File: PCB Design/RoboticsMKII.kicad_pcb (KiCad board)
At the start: 4 copper layers, 93 parts, among them CON1 USB, CON2 BARREL_JACK, P1 Power Sel, P10 CONN_02X12, P11 DAC, P12 Reed, P13 SPI, P14 ICSP, P15 Gnd, P16 UART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

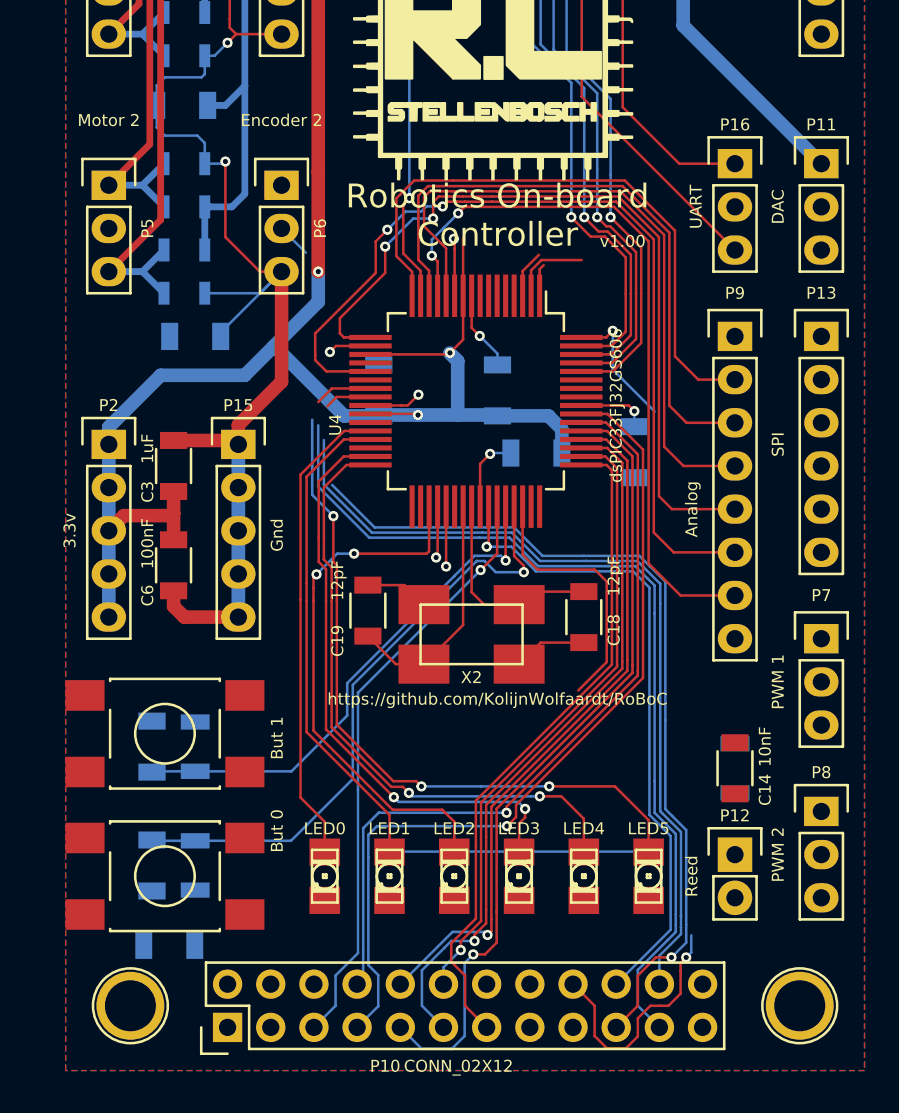
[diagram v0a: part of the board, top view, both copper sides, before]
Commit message: More done. PWM and SPI need attention
Signed-off-by: Kolijn Wolfaardt <kolijn.wolfaardt@gmail.com>
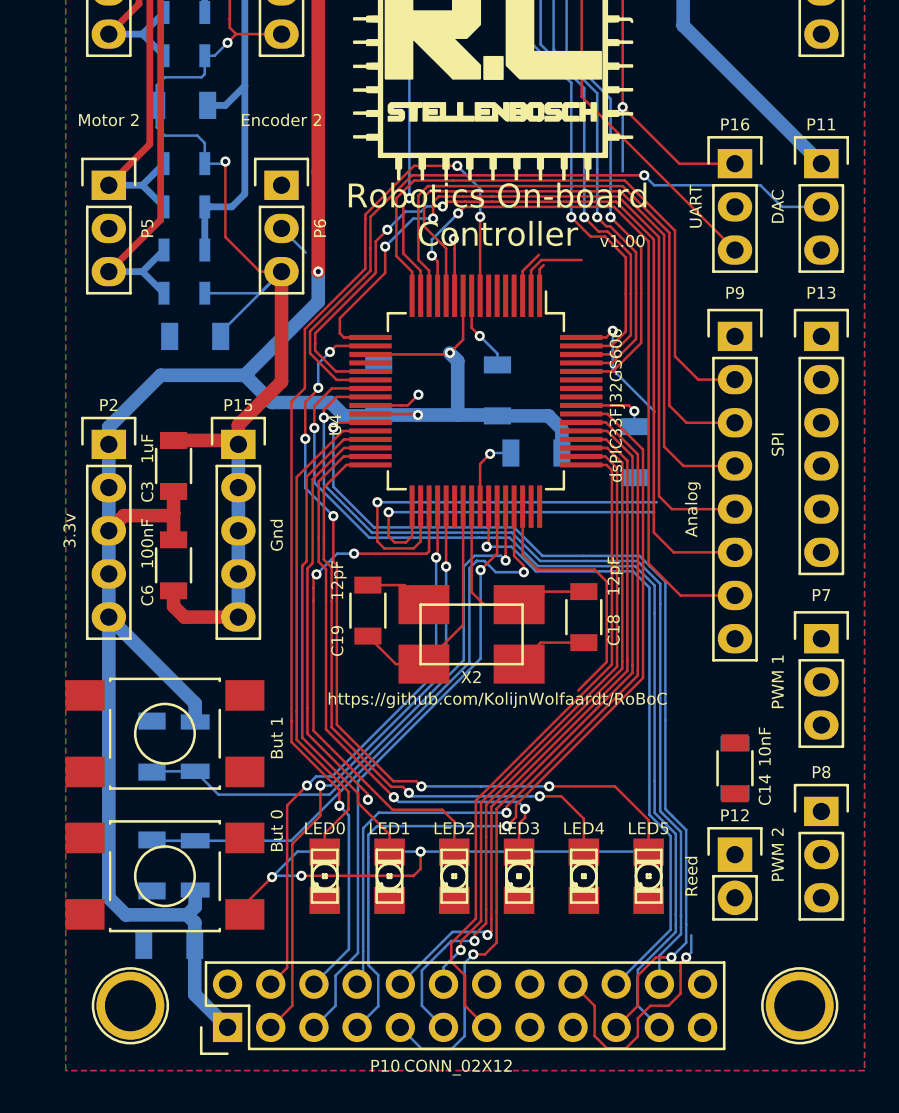
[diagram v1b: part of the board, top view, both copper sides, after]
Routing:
- net /gpio/Href: track 0.00 -> 64.1 mm, vias 0 -> 3
- net /gpio/DACOUT: track 0.00 -> 42.0 mm, vias 0 -> 1
- net V3.3: track 258.2 -> 294.9 mm
- net /gpio/SIO_C: track 3.53 -> 35.3 mm, vias 1 -> 2
- net /gpio/SIO_D: track 3.05 -> 32.7 mm, vias 1 -> 2
- net /usb/MCU_RX: track 28.2 -> 55.6 mm, vias 1 -> 3
- net /gpio/Reed: track 0.00 -> 24.6 mm, vias 0 -> 1
- net /usb/MCU_TX: track 33.5 -> 53.9 mm, vias 1 -> 2
- net GND: track 237.0 -> 254.1 mm, vias 14 -> 17
- net /gpio/~WR: track 50.9 -> 56.6 mm, vias 1 -> 2
- net /gpio/LED5: track 44.1 -> 48.9 mm, vias 4 -> 6
- net /gpio/BUT_1: track 30.5 -> 33.7 mm
- net /gpio/~RRST: track 52.2 -> 54.2 mm, vias 0 -> 1
- net /gpio/~WRST: track 57.2 -> 58.7 mm, vias 0 -> 1
- net /gpio/LED0: track 28.0 -> 29.4 mm

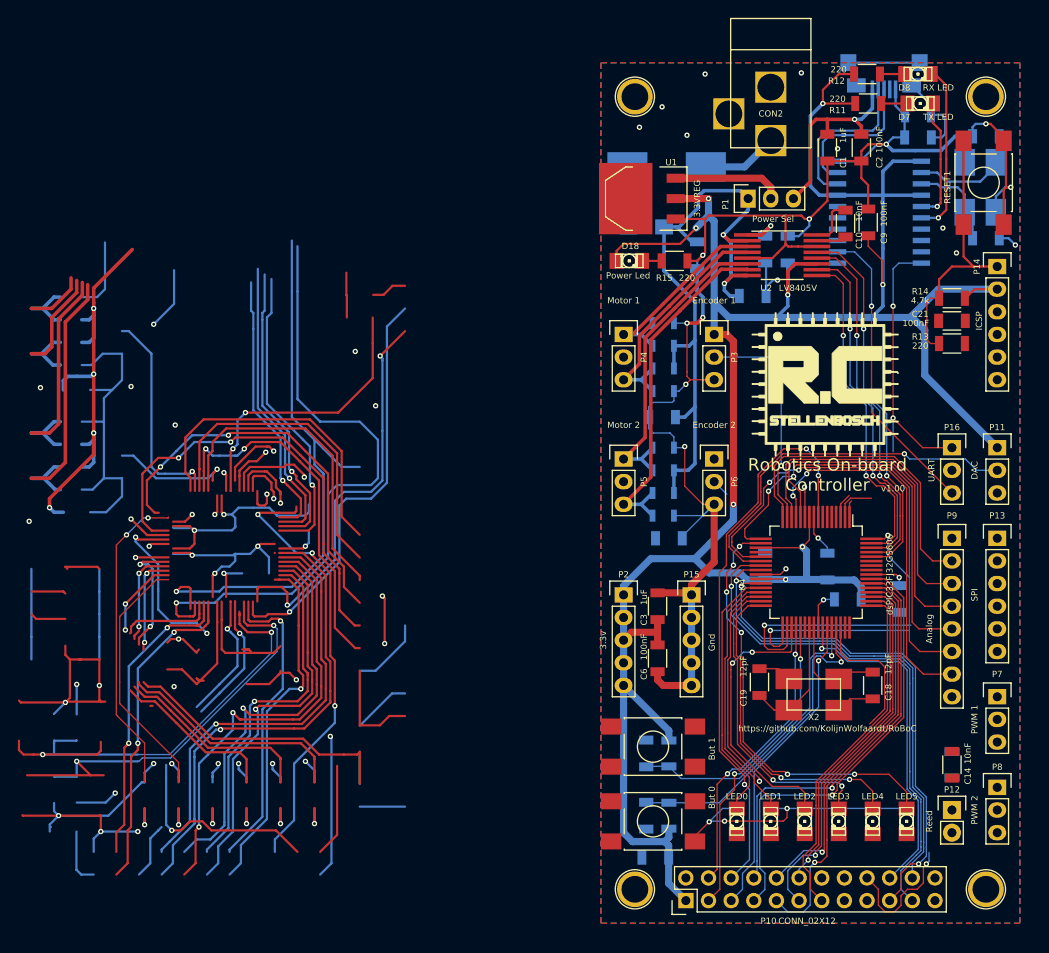
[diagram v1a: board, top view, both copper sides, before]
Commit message: Finished 2-layer routing, now it needs to be checked
Signed-off-by: Kolijn Wolfaardt <kolijn.wolfaardt@gmail.com>
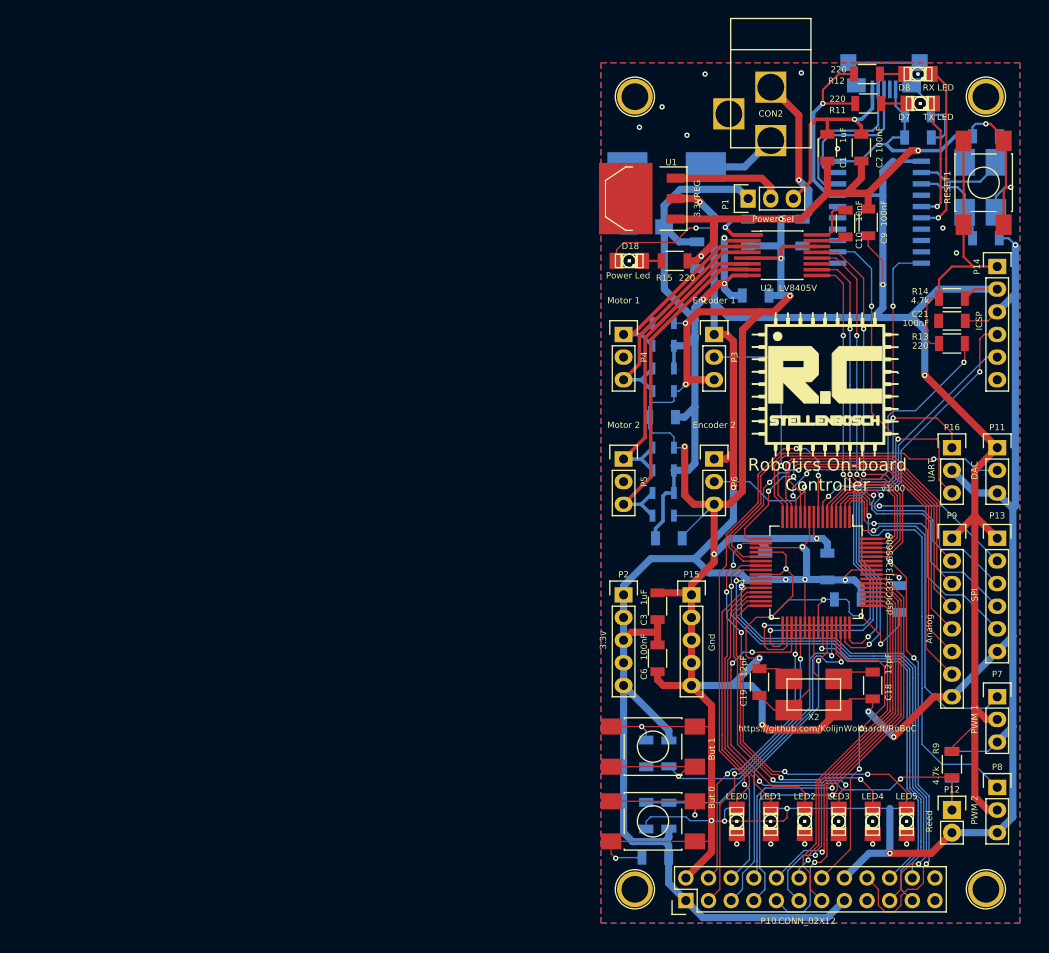
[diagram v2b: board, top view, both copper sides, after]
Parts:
- C14: moved to B.Cu
- R9: moved to F.Cu
- moved C11 2.69 mm to (129.5, 62.2)
- moved C4 2.52 mm to (135.6, 62.2)
- moved C22 0.33 mm to (130.4, 69.3)
- moved R9 0.05 mm to (152.4, 121.9)
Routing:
- net (no net): track 3276.9 -> 0.00 mm, vias 117 -> 8
- net GND: track 254.1 -> 589.9 mm, vias 17 -> 29
- net V3.3: track 294.9 -> 364.4 mm, vias 8 -> 10
- net /mcu/PGD: track 0.00 -> 49.7 mm, vias 0 -> 2
- net /motors/PWM2: track 2.81 -> 49.2 mm, vias 0 -> 1
- net /mcu/PGC: track 0.00 -> 45.3 mm, vias 0 -> 1
- net /motors/PWM1: track 1.90 -> 40.4 mm, vias 0 -> 1
- net /gpio/RCK: track 22.4 -> 54.1 mm, vias 2 -> 4
- net /gpio/Reed: track 24.6 -> 54.6 mm, vias 1 -> 2
- net /gpio/SPI_MISO: track 0.00 -> 29.9 mm, vias 0 -> 1
- net /mcu/MCLR: track 0.00 -> 29.7 mm, vias 0 -> 2
- net /gpio/SPI_MOSI: track 0.00 -> 28.9 mm, vias 0 -> 1
- net /gpio/SPI_SS: track 4.72 -> 29.2 mm, vias 0 -> 1
- net /usb/MCU_TX: track 53.9 -> 77.6 mm, vias 2 -> 3
- net /gpio/SPI_CLK: track 0.00 -> 23.5 mm, vias 0 -> 1
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- removed copper zone on In1.Cu, net GND
- removed copper zone on In2.Cu, net GND
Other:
- copper layers 4 -> 2

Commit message: 2layers almost done. Silkscreen needs checking
Signed-off-by: Kolijn Wolfaardt <kolijn.wolfaardt@gmail.com>
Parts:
- removed the G*** at (138.2, 79.2)
- added G***: LOGO, RoBoC:RoBoC_Logo__1700, F.Cu at (134.6, 79.2)
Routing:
- net V3.3: track 364.4 -> 382.4 mm, vias 10 -> 11
- net GND: track 589.9 -> 590.0 mm, vias 29 -> 30
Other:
- board text added: "v1.1"
- board text removed: "v1.00"

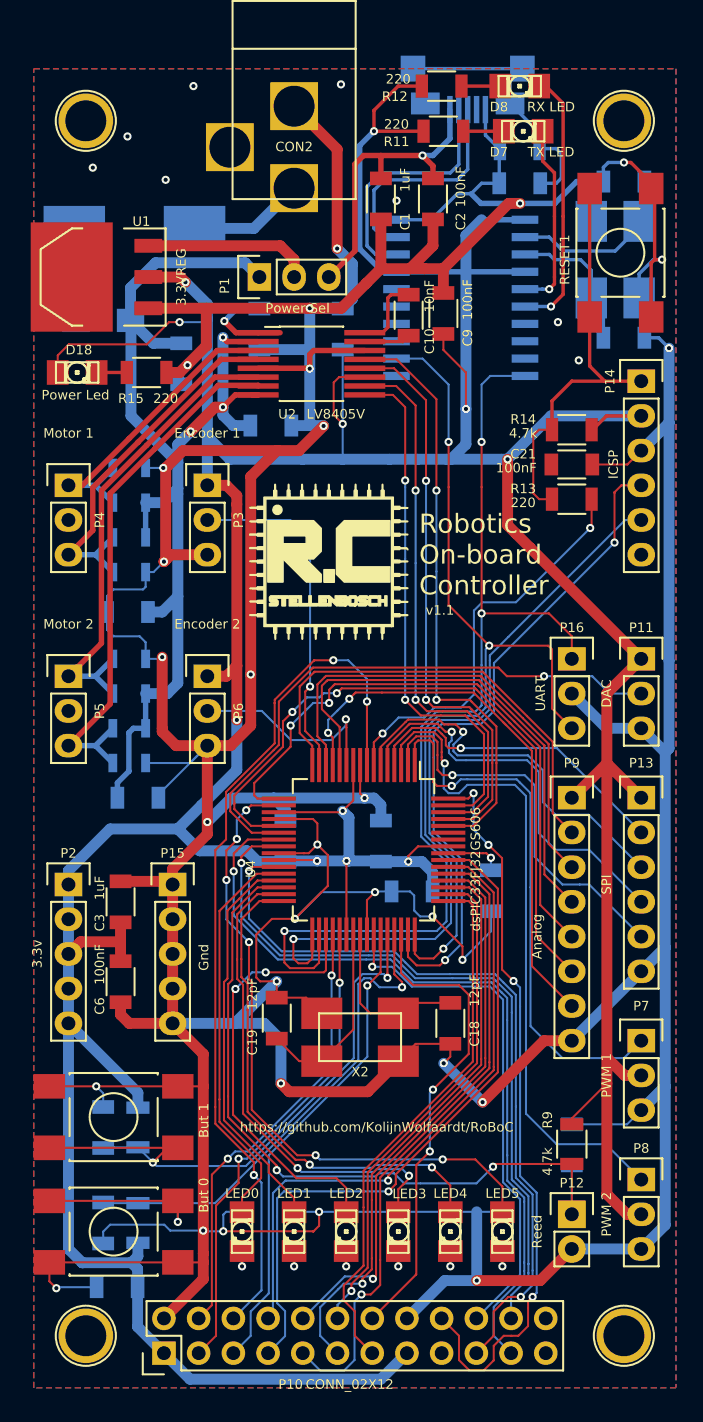
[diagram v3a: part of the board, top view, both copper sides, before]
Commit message: Top Silkscreen fixed. Almost done
Signed-off-by: Kolijn Wolfaardt <kolijn.wolfaardt@gmail.com>
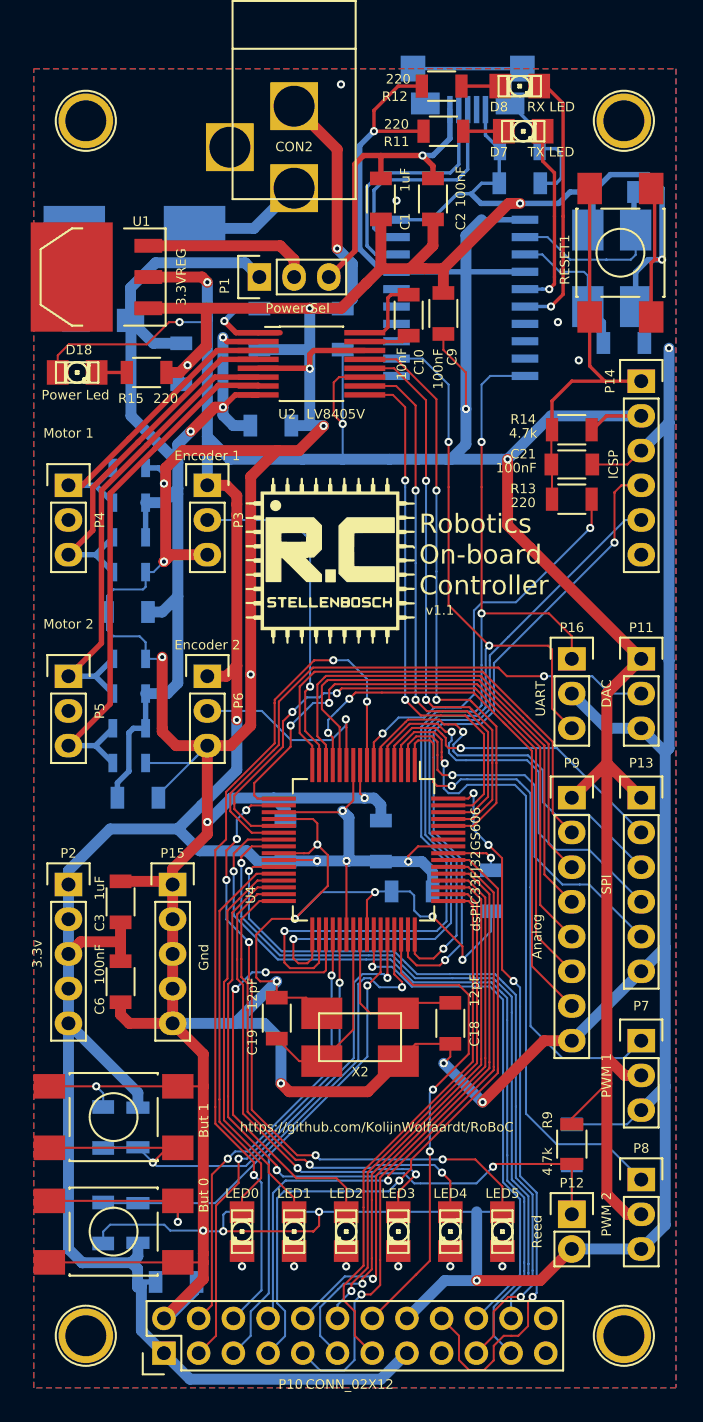
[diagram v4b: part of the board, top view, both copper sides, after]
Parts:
- removed the G*** at (134.6, 79.2)
- added G***: LOGO, RoBoC:RoBoC_Logo, F.Cu at (134.7, 79.2)
- moved C5 4.33 mm to (123.4, 132.0), turned to 0 degrees
- moved C15 1.08 mm to (155.4, 52.2)
- moved X1 0.68 mm to (155.3, 57.8)
- moved C16 0.38 mm to (156.2, 63.2)
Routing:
- net V3.3: track 382.4 -> 385.4 mm
- net /mcu/MCLR_in: track 31.2 -> 29.0 mm
- net GND: track 590.0 -> 591.7 mm, vias 30 -> 28
- net /gpio/LED3: track 35.6 -> 36.6 mm
- net /usb/USB_OSC1: track 13.0 -> 13.6 mm
- net (no net): vias 8 -> 4

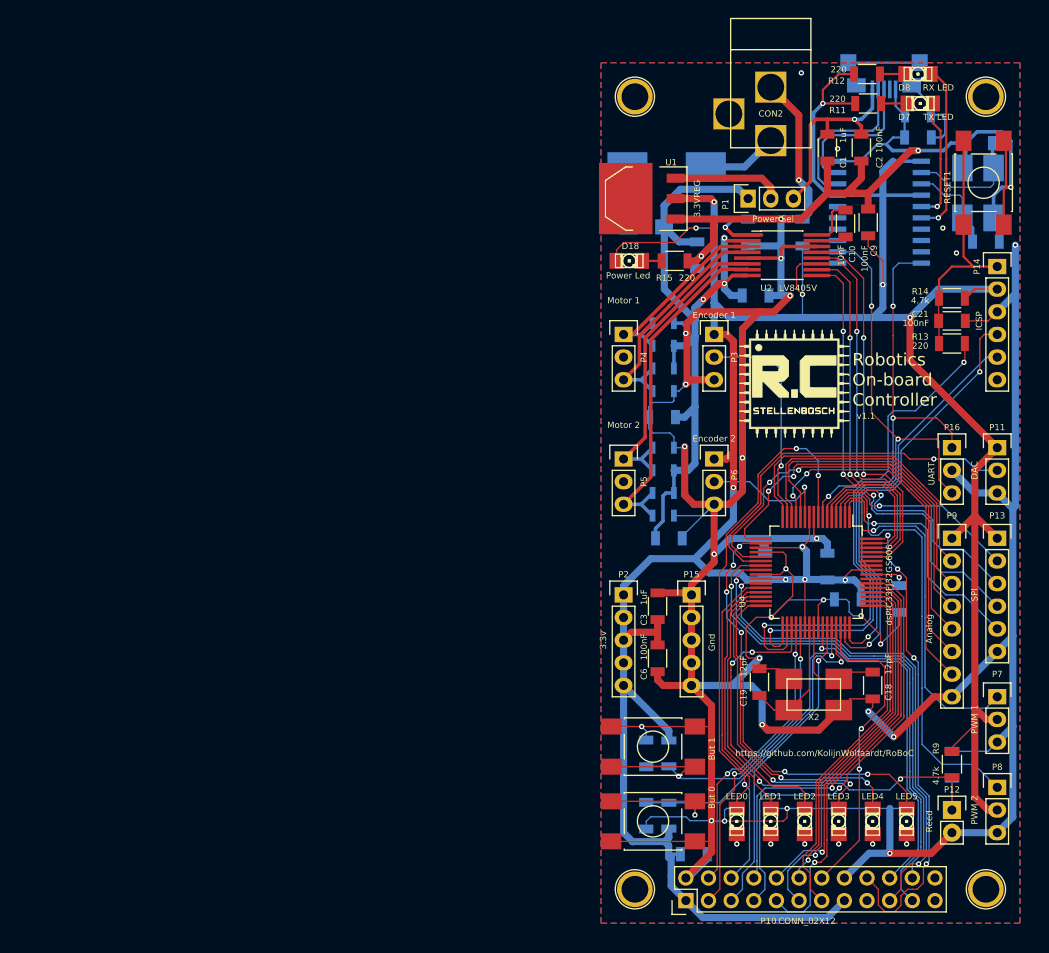
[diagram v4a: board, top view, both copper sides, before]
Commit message: Changed all via sizes, changed layout, changed jack footprint to original
Signed-off-by: Kolijn Wolfaardt <kolijn.wolfaardt@gmail.com>
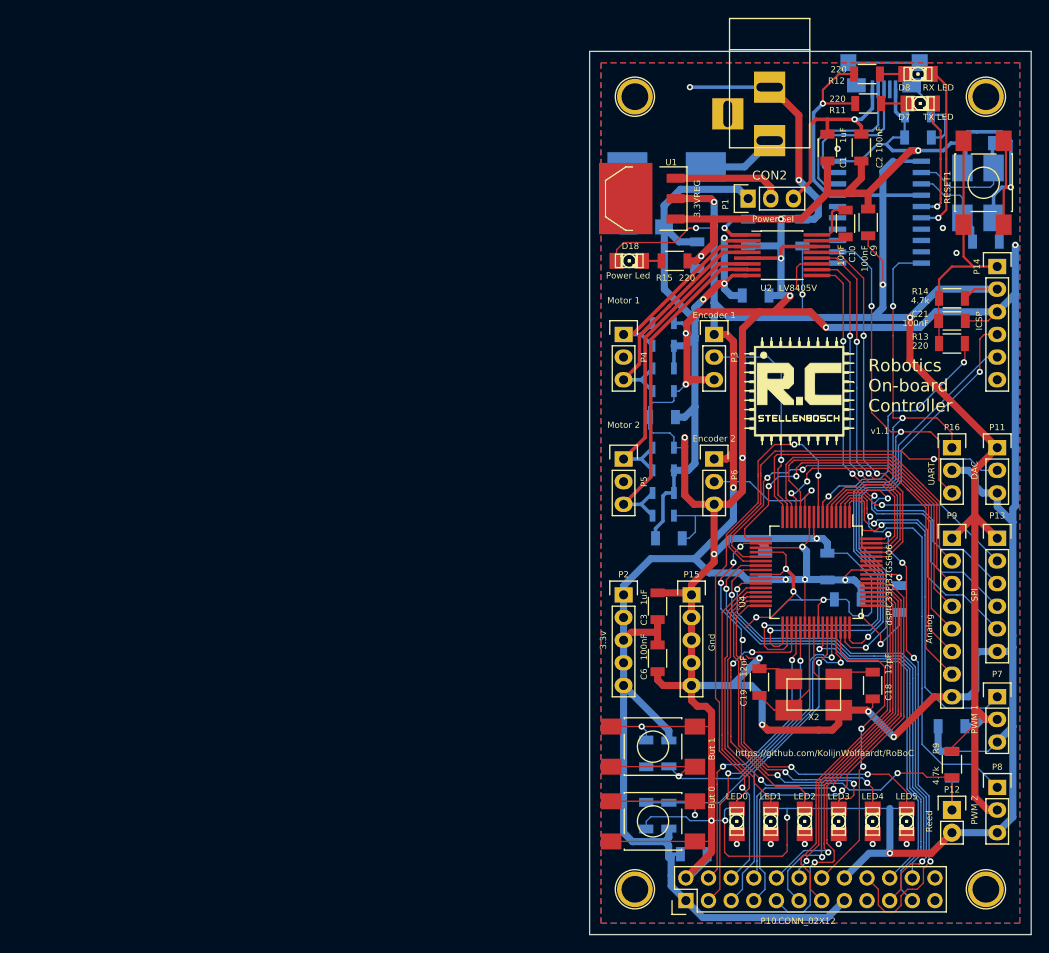
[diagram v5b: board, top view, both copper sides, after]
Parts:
- added C27: 1uF, Capacitors_SMD:C_1206, B.Cu at (152.3, 117.6)
- moved G*** 3.02 mm to (137.2, 79.2)
- moved G*** 1.01 mm to (135.3, 80.0)
- moved CON2 0.13 mm to (132.0, 45.7)
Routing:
- net GND: track 591.7 -> 657.4 mm, vias 28 -> 31
- net V3.3: track 385.4 -> 389.3 mm
- net /usb/MCU_TX: track 77.6 -> 79.8 mm
- net /gpio/Href: track 64.2 -> 66.0 mm
- net /usb/MCU_RX: track 75.3 -> 77.0 mm
- net /motors/VG: track 7.37 -> 5.92 mm
- net /gpio/DATA_5: track 46.8 -> 48.3 mm
- net /gpio/SPI_MOSI: track 28.9 -> 30.3 mm
- net /gpio/LED3: track 36.6 -> 37.6 mm
- net /mcu/MOT1_D1: track 43.6 -> 42.6 mm
- net /gpio/DATA_4: track 41.0 -> 42.0 mm
- net /gpio/DACOUT: track 42.0 -> 42.9 mm
- net /mcu/MOT1_D2: track 42.1 -> 41.2 mm
- net /gpio/DATA_3: track 42.2 -> 43.0 mm
- net /gpio/SIO_D: track 32.7 -> 33.5 mm
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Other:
- board outline added: 49.5 x 99.1 mm
- net class Default: via_dia 0.6 -> 0.7
- net class Heavy Power: via_dia 0.6 -> 0.7
- net class Power: via_dia 0.6 -> 0.7
- rule via_min_drill: 0.3 -> 0.4
- rule via_min_size: 0.4 -> 0.7
